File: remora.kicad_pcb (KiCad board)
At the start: 2 copper layers, 66 x 86 mm, 111 parts, among them J1 ST_01x03, J2 ST_01x02, J3 ST_01x02, J4 ST_01x02, J5 ST_01x02, J6 ST_01x02, J7 Conn_01x05_Pin, J8 RJ45_HanRun_HR911105A, J9 ST_01x02, K1 G5Q-1, Q1 MMBT2222, Q2 BSS138, U1 TLP267J, U10 TLP267J, U11 TLP267J, U12 TLP267J, U13 TLP267J, U14 TLP267J, U15 MCP23017_SO, U16 ESP32-D1-MINI, U17 LTV-814S, U2 TLP267J, U201 LAN8720A, U3 TLP267J, U4 TLP267J, U5 TLP267J, U6 TLP267J, U7 TLP267J, U8 TLP267J, U9 TLP267J, X201 50M

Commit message: Add Switch
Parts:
- added SW1: SW_Push, Button_Switch_SMD:SW_Push_1P1T_NO_6x6mm_H9.5mm, F.Cu at (112.1, 74.2)
- moved R22 4.03 mm to (108.0, 68.9), turned to 180 degrees
- moved R21 3.96 mm to (106.7, 78.7), turned to 180 degrees
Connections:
- U16 pad 5: unconnected-(U16-IO12/TDI-Pad5) -> Net-(U16-IO12/TDI)
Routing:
- net Net-(U16-IO12/TDI): track 0.00 -> 38.1 mm
- net /I2C_SDA: track 61.7 -> 70.2 mm
- net /I2C_SCL: track 64.3 -> 70.5 mm
- net +3V3: track 226.0 -> 231.5 mm, vias 12 -> 11
- net GND: track 21.1 -> 23.9 mm, vias 146 -> 25

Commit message: Modif commande v2.0
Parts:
- C3: footprint Capacitor_THT:C_Rect_L10.0mm_W4.0mm_P7.50mm_MKS4 -> Capacitor_THT:C_Rect_L11.5mm_W5.6mm_P10.00mm_MKT
- U201: footprint Package_DFN_QFN:VQFN-24-1EP_4x4mm_P0.5mm_EP2.5x2.5mm_ThermalVias -> Package_DFN_QFN:VQFN-24-1EP_4x4mm_P0.5mm_EP2.5x2.5mm
- moved C3 0.50 mm to (149.7, 92.5)
- moved R18 0.31 mm to (144.6, 93.4)
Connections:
- SW1 pad 1: Net-(U16-IO12/TDI) -> Net-(U16-IO16)
- U16 pad 16: unconnected-(U16-IO16-Pad16) -> Net-(U16-IO16)
- U16 pad 5: Net-(U16-IO12/TDI) -> unconnected-(U16-IO12/TDI-Pad5)
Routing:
- net Net-(U16-IO16): track 0.00 -> 40.6 mm
- net Net-(U16-IO12/TDI): track 38.1 -> 0.00 mm
- net /RL_SNUB: track 6.97 -> 5.85 mm
- net /RL_OUT: track 16.3 -> 16.9 mm
- net GND: vias 25 -> 146

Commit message: Mise a jour 1er assemblage
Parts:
- removed REF**: OSHW-Logo_5.7x6mm_SilkScreen, Symbol:OSHW-Logo_5.7x6mm_SilkScreen
- R211, R213: value 330R -> 120R
- R23: value 100R -> 330R

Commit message: Fix transistor relai (collecteur et émeteur intervertis)
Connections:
- Q1 pad 2: /RL_TE -> GND
- Q1 pad 3: GND -> /RL_TE
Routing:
- net /RL_TE: track 7.20 -> 9.42 mm
- net GND: track 23.9 -> 24.8 mm, vias 146 -> 145
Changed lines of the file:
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@@
       (net 45 "/RL_TB") (pinfunction "B") (pintype "input"))
     (pad "2" smd roundrect (at -0.9375 0.95) (size 1.475 0.6) (layers "F.Cu" "F.Paste" "F.Mask") (roundrect_rratio 0.25)
-      (net 27 "/RL_TE") (pinfunction "E") (pintype "passive"))
+      (net 2 "GND") (pinfunction "E") (pintype "passive"))
     (pad "3" smd roundrect (at 0.9375 0) (size 1.475 0.6) (layers "F.Cu" "F.Paste" "F.Mask") (roundrect_rratio 0.25)
-      (net 2 "GND") (pinfunction "C") (pintype "passive"))
+      (net 27 "/RL_TE") (pinfunction "C") (pintype "passive"))
     (model "${KICAD6_3DMODEL_DIR}/Package_TO_SOT_SMD.3dshapes/SOT-23.wrl"
       (offset (xyz 0 0 0))
@@
   (segment (start 133.745 69.35) (end 133.745 67.845) (width 0.2) (layer "F.Cu") (net 2))
   (segment (start 117.65 37.55) (end 117.65 38.9625) (width 0.2) (layer "F.Cu") (net 2))
-  (segment (start 161.9375 67.6) (end 163.5 67.6) (width 0.3) (layer "F.Cu") (net 2))
   (segment (start 130.3 80.3) (end 129.935 79.935) (width 0.2) (layer "F.Cu") (net 2))
   (segment (start 132.655 67.845) (end 133.745 67.845) (width 0.2) (layer "F.Cu") (net 2))
@@
   (segment (start 121.5 20.9) (end 121 21.4) (width 0.5) (layer "F.Cu") (net 2))
   (segment (start 124.4 20.9) (end 124.9 21.4) (width 0.5) (layer "F.Cu") (net 2))
+  (segment (start 157.65 68.55) (end 157.6 68.6) (width 0.25) (layer "F.Cu") (net 2))
   (segment (start 134.6 66.4) (end 133.3375 66.4) (width 0.2) (layer "F.Cu") (net 2))
   (segment (start 131.3 80.3) (end 130.3 80.3) (width 0.2) (layer "F.Cu") (net 2))
@@
   (segment (start 129.935 79.935) (end 129.935 78.65) (width 0.2) (layer "F.Cu") (net 2))
   (segment (start 122.9 20.9) (end 121.5 20.9) (width 0.5) (layer "F.Cu") (net 2))
+  (segment (start 160.0625 68.55) (end 157.65 68.55) (width 0.25) (layer "F.Cu") (net 2))
   (segment (start 122.9 23.1625) (end 122.9 20.9) (width 0.5) (layer "F.Cu") (net 2))
   (segment (start 135.015 69.35) (end 135.015 68.015) (width 0.2) (layer "F.Cu") (net 2))
@@
   (via (at 150.725 69.165) (size 0.8) (drill 0.4) (layers "F.Cu" "B.Cu") (free) (net 2))
   (via (at 132.945 31.065) (size 0.8) (drill 0.4) (layers "F.Cu" "B.Cu") (free) (net 2))
-  (via (at 163.5 67.6) (size 0.7) (drill 0.3) (layers "F.Cu" "B.Cu") (net 2))
   (via (at 124.9 21.4) (size 0.9) (drill 0.4) (layers "F.Cu" "B.Cu") (net 2))
   (via (at 115.165 36.145) (size 0.8) (drill 0.4) (layers "F.Cu" "B.Cu") (free) (net 2))
@@
   (segment (start 136.57 92.15) (end 136.57 94.47) (width 0.8) (layer "B.Cu") (net 26))
   (segment (start 136.57 94.47) (end 136.7 94.6) (width 0.8) (layer "B.Cu") (net 26))
-  (segment (start 160.0625 68.55) (end 160.0625 71.1475) (width 0.3) (layer "F.Cu") (net 27))
+  (segment (start 160.9 71.2) (end 160.115 71.2) (width 0.25) (layer "F.Cu") (net 27))
   (segment (start 160.0625 71.1475) (end 160.115 71.2) (width 0.2) (layer "F.Cu") (net 27))
+  (segment (start 161.9375 67.6) (end 161.9375 70.1625) (width 0.25) (layer "F.Cu") (net 27))
   (segment (start 160.115 71.2) (end 160.115 72.305) (width 0.3) (layer "F.Cu") (net 27))
   (segment (start 160.115 72.305) (end 162.535 74.725) (width 0.3) (layer "F.Cu") (net 27))
+  (segment (start 161.9375 70.1625) (end 160.9 71.2) (width 0.25) (layer "F.Cu") (net 27))
   (segment (start 137.6 75.5) (end 141.875 71.225) (width 0.2) (layer "F.Cu") (net 28))
   (segment (start 127.395 79.995) (end 128.5 81.1) (width 0.2) (layer "F.Cu") (net 28))

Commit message: Deplacement du pin teleinfo de SD1 à GPIO13
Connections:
- U16 pad 29: unconnected-(U16-IO13/TCK-Pad29) -> /TELEINFO
- U16 pad 9: /TELEINFO -> unconnected-(U16-SD1/SDI-Pad9)
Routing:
- net /TELEINFO: track 23.4 -> 40.5 mm, vias 0 -> 2

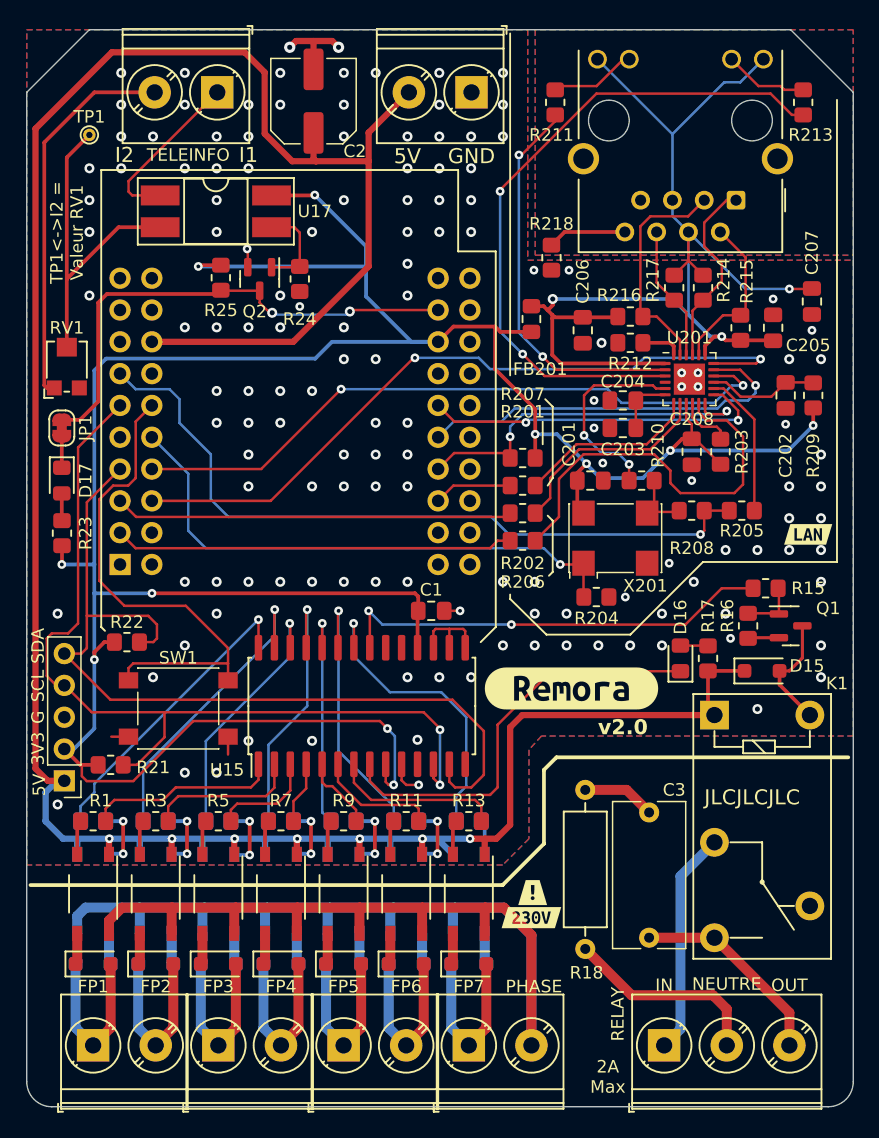
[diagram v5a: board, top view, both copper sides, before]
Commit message: Nouvelles empreintes pour les diodes
Les pads des diodes ont été agrandies et espacées pour respecter la datasheet.
Changement ref des borniers pour du 2.5mm²
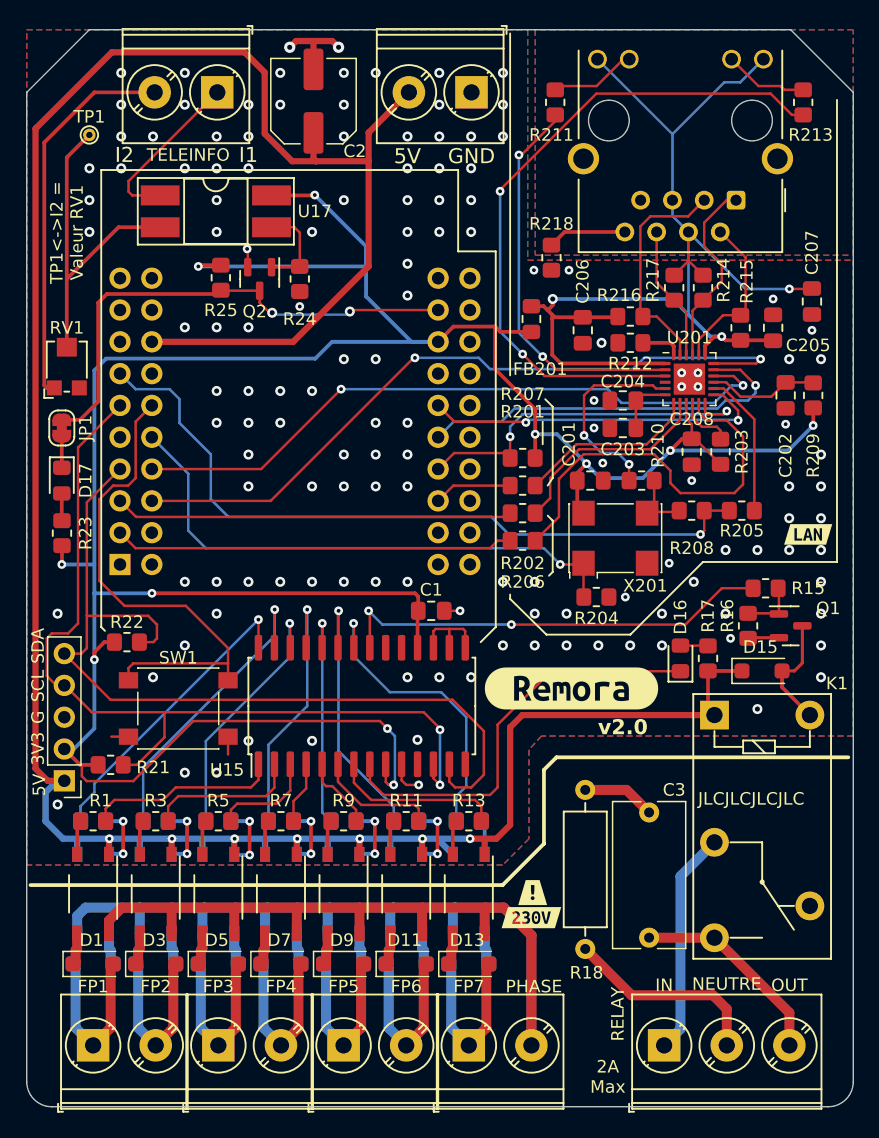
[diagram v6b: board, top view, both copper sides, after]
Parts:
- added REF**: OSHW-Logo_11.4x12mm_SilkScreen, Symbol:OSHW-Logo_11.4x12mm_SilkScreen, B.Cu at (158.8, 65.6)
- D1, D10, D11, D12, D13, D14, D15, D2, D3, D4, D5, D6, D7, D8, D9: footprint Diode_SMD:D_SOD-123F -> remora_lib:D_SOD-123FL
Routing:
- net GND: vias 145 -> 142
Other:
- board text added: "JLCJLCJLCJLC"
- board text removed: "JLCJLCJLC"

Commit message: Version 2.0 r1
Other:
- board text added: "r1"
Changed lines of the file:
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@@
+		)
+	)
+	(gr_text "r1"
+		(at 151.3 76.3 0)
+		(layer "F.SilkS")
+		(effects
+			(font
+				(size 1 1)
+				(thickness 0.2)
+				(bold yes)
+			)
+			(justify right bottom)
 		)
 	)
